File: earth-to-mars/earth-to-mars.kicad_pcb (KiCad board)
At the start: 2 copper layers, 36 x 42 mm, 10 parts, among them P10 CONN_01X06, P6 CONN_01X04, P7 CONN_01X06, P8 CONN_01X04, Q1 Q_NMOS_DGS, U1 mq8, U2 dht11

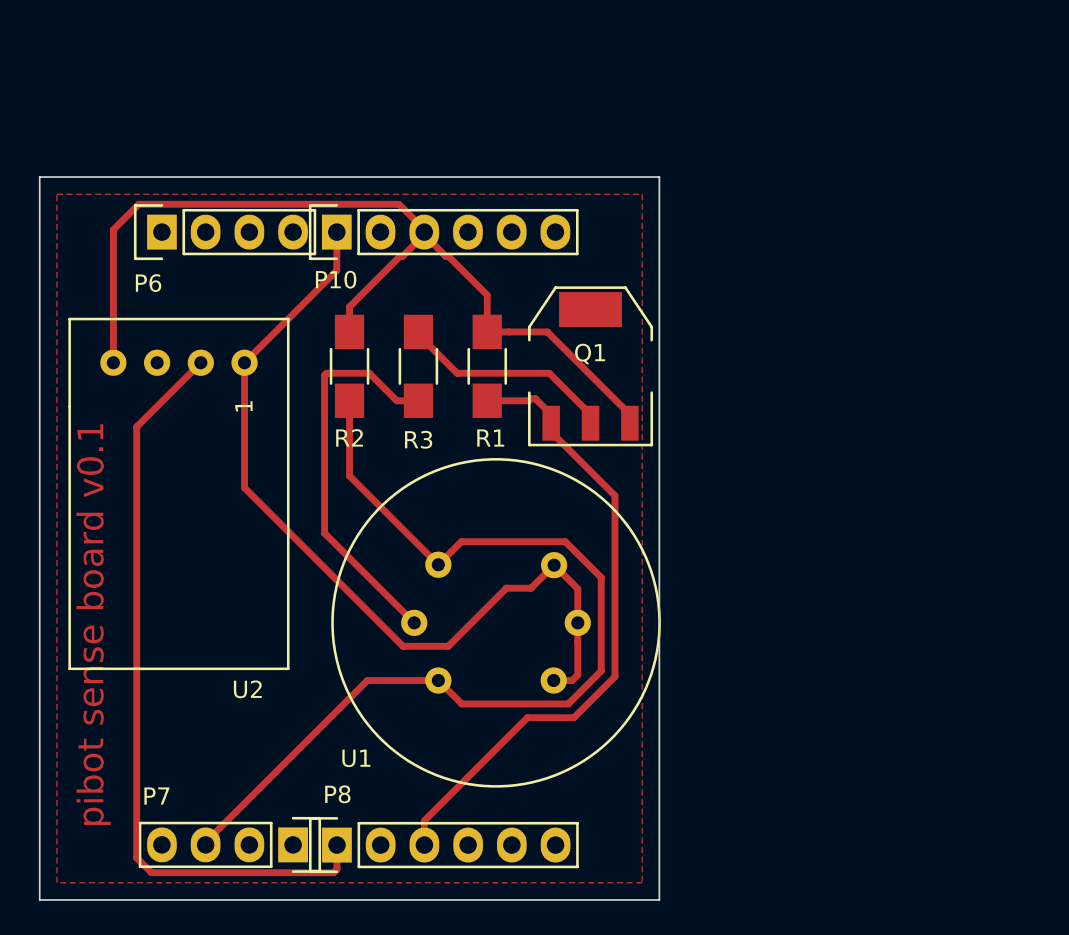
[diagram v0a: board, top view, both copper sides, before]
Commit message: flying lead configuration
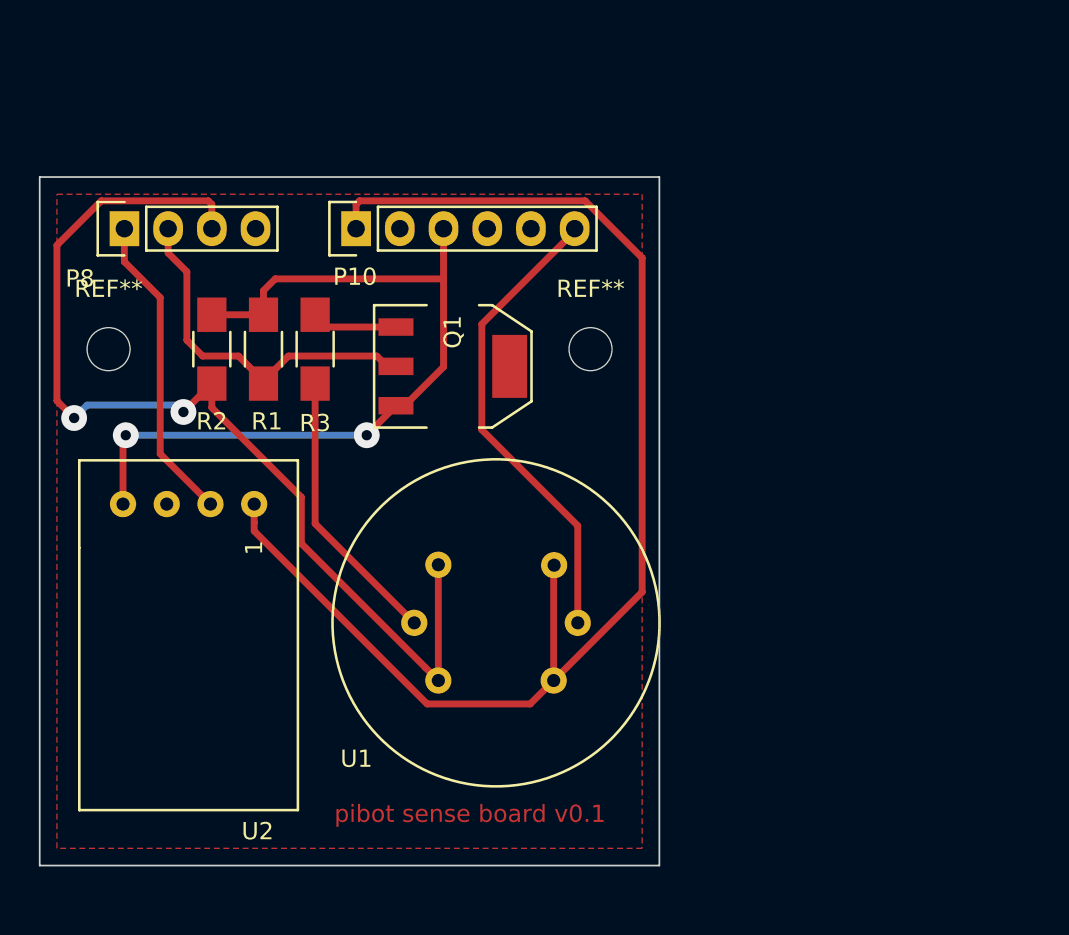
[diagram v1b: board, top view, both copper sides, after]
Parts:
- removed P6: CONN_01X04, Pin_Headers:Pin_Header_Straight_1x04
- removed P7: CONN_01X06, Pin_Headers:Pin_Header_Straight_1x06
- added REF**: MountingHole_2-5mm, Mounting_Holes:MountingHole_2-5mm, F.Cu at (113.0, 97.0)
- added REF**: MountingHole_2-5mm, Mounting_Holes:MountingHole_2-5mm, F.Cu at (141.0, 97.0)
- Q1: footprint fp:SOT-223 -> TO_SOT_Packages_SMD:SOT-223
- moved P8 37.1 mm to (113.9, 90.0), turned to 90 degrees
- moved R1 13.0 mm to (122.0, 97.0)
- moved U2 8.23 mm to (111.3, 106.0)
- moved R2 8.06 mm to (119.0, 97.0)
- moved Q1 8.00 mm to (133.0, 98.0), turned to 270 degrees
- moved R3 6.08 mm to (125.0, 97.0)
- moved P10 1.14 mm to (127.4, 90.0)
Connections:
- P10 pad 6: (no net) -> +BATT
- P8 pad 1: (no net) -> mega_adc4_sda
- P8 pad 2: (no net) -> mega_adc5_scl
- Q1 pad 2: mega_io13_sck -> mega_adc5_scl
- R1 pad 1: mega_io13_sck -> mega_adc5_scl
- U1 pad 2: +5V -> +BATT
- U2 pad 2: mega_io12_miso -> mega_adc4_sda
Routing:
- net mega_io12_miso: track 43.8 -> 0.00 mm
- net mega_io13_sck: track 36.9 -> 0.00 mm
- net +BATT: track 0.00 -> 27.4 mm
- net +5V: track 49.3 -> 76.6 mm
- net mega_adc5_scl: track 0.00 -> 21.1 mm
- net mega_adc4_sda: track 0.00 -> 18.1 mm
- net Net-(Q1-Pad1): track 12.6 -> 4.99 mm
- net Net-(R3-Pad1): track 22.7 -> 16.3 mm
- net Earth: track 52.9 -> 47.4 mm, vias 0 -> 2
- net mega_adc6: track 56.4 -> 60.6 mm, vias 0 -> 2
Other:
- board size 36 x 42 mm -> 36 x 40 mm

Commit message: fixed mosfet fp and added header for vbat=vcc
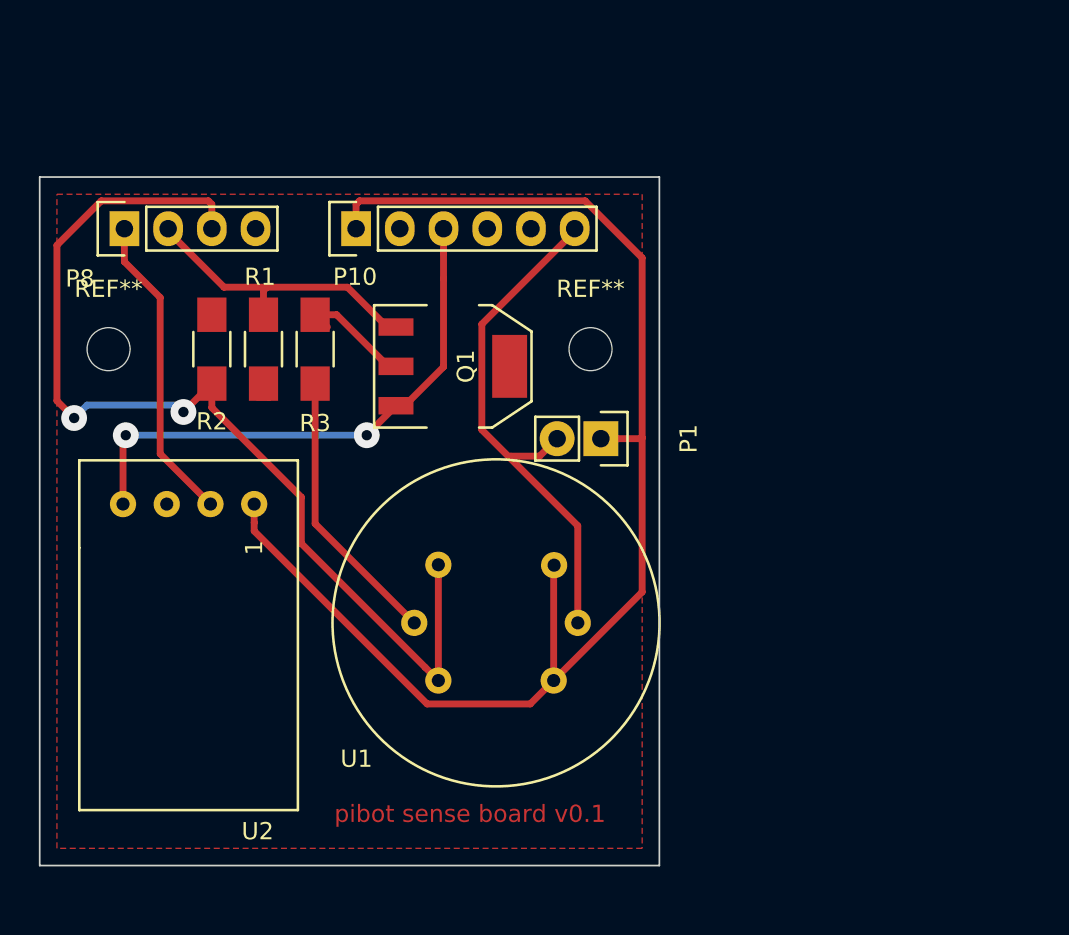
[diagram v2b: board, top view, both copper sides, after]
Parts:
- added P1: CONN_01X02, Pin_Headers:Pin_Header_Straight_1x02, F.Cu at (141.6, 102.2)
- Q1: footprint TO_SOT_Packages_SMD:SOT-223 -> fp:SOT-223
- turned R1 to 270 degrees
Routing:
- net Earth: track 47.4 -> 33.4 mm
- net mega_adc5_scl: track 21.1 -> 17.4 mm
- net +BATT: track 27.4 -> 30.7 mm
- net Net-(Q1-Pad1): track 4.99 -> 7.46 mm
- net +5V: track 76.6 -> 79.0 mm

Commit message: switched pins for working PWM, aligned header for direct connection
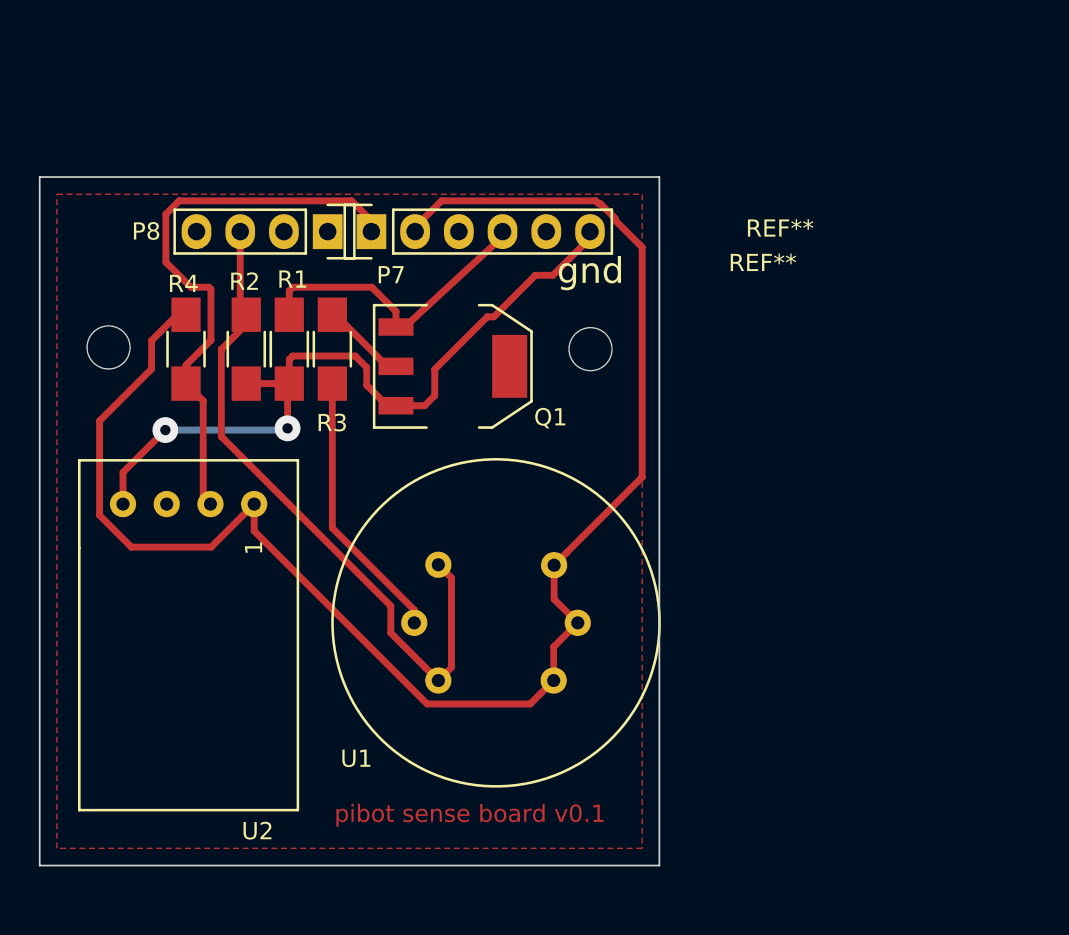
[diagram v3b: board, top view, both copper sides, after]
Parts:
- removed P1: CONN_01X02, Pin_Headers:Pin_Header_Straight_1x02
- removed P10: CONN_01X06, Pin_Headers:Pin_Header_Straight_1x06
- added P7: CONN_01X06, Pin_Headers:Pin_Header_Straight_1x06, F.Cu at (128.3, 90.2)
- added R4: 4.7k, Resistors_SMD:R_1206_HandSoldering, F.Cu at (117.5, 97.0)
- R1: value R -> 10k
- R2: value R -> 4.7k
- R3: value R -> 5R
- moved P8 11.8 mm to (125.7, 90.2), turned to 270 degrees
- moved R2 2.00 mm to (121.0, 97.0), turned to 270 degrees
- moved R1 1.50 mm to (123.5, 97.0)
- moved R3 1.00 mm to (126.0, 97.0)
- moved REF** 0.10 mm to (113.0, 96.9)
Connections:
- P8 pad 1: mega_adc4_sda -> (no net)
- P8 pad 2: mega_adc5_scl -> (no net)
- Q1 pad 2: mega_adc5_scl -> mega_io11_mosi
- R1 pad 1: mega_adc5_scl -> mega_io11_mosi
- U1 pad 2: +BATT -> +5V
- U2 pad 2: mega_adc4_sda -> mega_io12_miso
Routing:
- net mega_io12_miso: track 0.00 -> 33.1 mm
- net +BATT: track 30.7 -> 0.00 mm
- net mega_adc6: track 60.6 -> 39.4 mm, vias 2 -> 0
- net mega_adc4_sda: track 18.1 -> 0.00 mm
- net mega_io11_mosi: track 0.00 -> 17.7 mm
- net mega_adc5_scl: track 17.4 -> 0.00 mm
- net +5V: track 79.0 -> 92.2 mm
- net Earth: track 33.4 -> 43.7 mm
- net Net-(Q1-Pad1): track 7.46 -> 4.94 mm
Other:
- board text added: "gnd"

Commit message: added cap
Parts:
- added C1: 4.7uf, Capacitors_SMD:c_elec_4x4.5, F.Cu at (112.9, 91.1)
- R1: value 10k -> 4k7
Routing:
- net +5V: track 92.2 -> 92.9 mm

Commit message: mq8 sensor board
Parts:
- removed R2: 4.7k, Resistors_SMD:R_1206_HandSoldering
- removed R3: 5R, Resistors_SMD:R_1206_HandSoldering
- removed the REF** at (113.0, 96.9)
- removed the REF** at (141.0, 97.0)
- removed U1: mq8, fp:mq8
- added P1: CONN_01X04, Pin_Headers:Pin_Header_Straight_1x04, F.Cu at (132.5, 99.0)
- added REF**: MountingHole_3-5mm, Mounting_Holes:MountingHole_3-5mm, F.Cu at (144.0, 94.8)
- added REF**: MountingHole_3-5mm, Mounting_Holes:MountingHole_3-5mm, F.Cu at (112.0, 94.8)
- moved C1 23.8 mm to (136.5, 94.5), turned to 180 degrees
- moved Q1 7.47 mm to (125.8, 96.0)
- moved R1 4.19 mm to (119.5, 95.8)
- moved U2 3.00 mm to (112.1, 103.1)
- moved R4 1.27 mm to (117.2, 95.8), turned to 90 degrees
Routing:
- net +5V: track 92.9 -> 40.8 mm
- net mega_adc6: track 39.6 -> 15.6 mm
- net Net-(R3-Pad1): track 15.9 -> 0.00 mm
- net Net-(P1-Pad3): track 4.94 -> 17.5 mm
- net Earth: track 43.7 -> 52.4 mm, vias 2 -> 1
- net mega_io12_miso: track 33.1 -> 25.3 mm
- net mega_io11_mosi: track 17.7 -> 18.0 mm, vias 0 -> 1
- removed copper zone on F.Cu, net Earth
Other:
- board size 36 x 40 mm -> 38 x 40 mm
- board text added: "ao"
- board text added: "dh11/22"
- board text added: "mq8"
- board text added: "vcc"
